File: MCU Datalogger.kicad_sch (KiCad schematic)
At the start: 0 parts

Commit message: symbols initialized
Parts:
- added BT?: Battery_Cell, symbol Device:Battery_Cell
- added C1, C2, C3, C?: C, symbol Device:C
- added C?: C_Polarized, symbol Device:C_Polarized
- added D1, D?: LED, symbol Device:LED
- added H1, H2, H3, H?: MountingHole, symbol Mechanical:MountingHole
- added R1, R2, R3, R4, R5, R6, R?: R, symbol Device:R
- added U1, U?: 24LC1025, symbol Memory_EEPROM:24LC1025
- added U?: ATMEGA328PB-AU, 32A_MCH, symbol 2025-06-18_17-37-05:ATMEGA328PB-AU
- added U?: DS1337S_, DS1337S_:SOIC127P600X175-8N, symbol DS1337S_:DS1337S_
- added Y1, Y?: Crystal, symbol Device:Crystal
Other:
- added sheet connnector sheet (connector.kicad_sch)

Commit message: symbols updated
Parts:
- removed U?: ATMEGA328PB-AU, 32A_MCH, symbol 2025-06-18_17-37-05:ATMEGA328PB-AU
- added U?: ATMEGA328P-AU, TQFP32_32A_MCH, symbol 2025-06-19_06-22-11:ATMEGA328P-AU
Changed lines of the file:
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@@
-	)
-	(symbol
-		(lib_id "2025-06-18_17-37-05:ATMEGA328PB-AU")
-		(at 143.51 46.99 0)
-		(unit 1)
-		(exclude_from_sim no)
-		(in_bom yes)
-		(on_board yes)
-		(dnp no)
-		(fields_autoplaced yes)
-		(property "Reference" "U?"
-			(at 209.55 36.83 0)
-			(effects
-				(font
-					(size 1.524 1.524)
-				)
-			)
-		)
-		(property "Value" "ATMEGA328PB-AU"
-			(at 209.55 39.37 0)
-			(effects
-				(font
-					(size 1.524 1.524)
-				)
-			)
-		)
-		(property "Footprint" "32A_MCH"
-			(at 143.51 46.99 0)
-			(effects
-				(font
-					(size 1.27 1.27)
-					(italic yes)
-				)
-				(hide yes)
-			)
-		)
-		(property "Datasheet" "ATMEGA328PB-AU"
-			(at 143.51 46.99 0)
-			(effects
-				(font
-					(size 1.27 1.27)
-					(italic yes)
-				)
-				(hide yes)
-			)
-		)
-		(property "Description" ""
-			(at 143.51 46.99 0)
-			(effects
-				(font
-					(size 1.27 1.27)
-				)
-				(hide yes)
-			)
-		)
-		(pin "9"
-		)
-		(pin "7"
-		)
-		(pin "2"
-		)
-		(pin "29"
-		)
-		(pin "27"
-		)
-		(pin "26"
-		)
-		(pin "3"
-		)
-		(pin "8"
-		)
-		(pin "1"
-		)
-		(pin "6"
-		)
-		(pin "4"
-		)
-		(pin "5"
-		)
-		(pin "11"
-		)
-		(pin "12"
-		)
-		(pin "13"
-		)
-		(pin "14"
-		)
-		(pin "15"
-		)
-		(pin "16"
-		)
-		(pin "32"
-		)
-		(pin "10"
-		)
-		(pin "31"
-		)
-		(pin "30"
-		)
-		(pin "28"
-		)
-		(pin "20"
-		)
-		(pin "23"
-		)
-		(pin "21"
-		)
-		(pin "19"
-		)
-		(pin "25"
-		)
-		(pin "18"
-		)
-		(pin "24"
-		)
-		(pin "22"
-		)
-		(pin "17"
-		)
-		(instances
-			(project ""
-				(path "/3b0fcfdb-a6be-445d-b7c4-9e7a0848a48e"
-					(reference "U?")
-					(unit 1)
-				)
-			)
-		)
 	)
 	(symbol
@@
 					(unit 1)
 				)
+			)
+		)
+	)
+	(symbol
+		(lib_id "2025-06-19_06-22-11:ATMEGA328P-AU")
+		(at 141.986 38.1 0)
+		(unit 1)
+		(exclude_from_sim no)
+		(in_bom yes)
+		(on_board yes)
+		(dnp no)
+		(fields_autoplaced yes)
+		(property "Reference" "U?"
+			(at 200.406 27.94 0)
+			(effects
+				(font
+					(size 1.524 1.524)
+				)
+			)
+		)
+		(property "Value" "ATMEGA328P-AU"
+			(at 200.406 30.48 0)
+			(effects
+				(font
+					(size 1.524 1.524)
+				)
+			)
+		)
+		(property "Footprint" "TQFP32_32A_MCH"
+			(at 141.986 38.1 0)
+			(effects
+				(font
+					(size 1.27 1.27)
+					(italic yes)
+				)
+				(hide yes)
+			)
+		)
+		(property "Datasheet" "ATMEGA328P-AU"
+			(at 141.986 38.1 0)
+			(effects
+				(font
+					(size 1.27 1.27)
+					(italic yes)
+				)
+				(hide yes)
+			)
+		)
+		(property "Description" ""
+			(at 141.986 38.1 0)
+			(effects
+				(font
+					(size 1.27 1.27)
+				)
+				(hide yes)
+			)
+		)
+		(pin "11"
+		)
+		(pin "5"
+		)
+		(pin "7"
+		)
+		(pin "1"
+		)
+		(pin "3"
+		)
+		(pin "9"
+		)
+		(pin "2"
+		)
+		(pin "4"
+		)
+		(pin "8"
+		)
+		(pin "6"
+		)
+		(pin "10"
+		)
+		(pin "12"
+		)
+		(pin "13"
+		)
+		(pin "14"
+		)
+		(pin "15"
+		)
+		(pin "16"
+		)
+		(pin "32"
+		)
+		(pin "31"
+		)
+		(pin "25"
+		)
+		(pin "29"
+		)
+		(pin "23"
+		)
+		(pin "21"
+		)
+		(pin "19"
+		)
+		(pin "20"
+		)
+		(pin "28"
+		)
+		(pin "18"
+		)
+		(pin "26"
+		)
+		(pin "17"
+		)
+		(pin "27"
+		)
+		(pin "24"
+		)
+		(pin "22"
+		)
+		(pin "30"
+		)
+		(instances
+			(project ""
+				(path "/3b0fcfdb-a6be-445d-b7c4-9e7a0848a48e"
+					(reference "U?")
+					(unit 1)
+				)

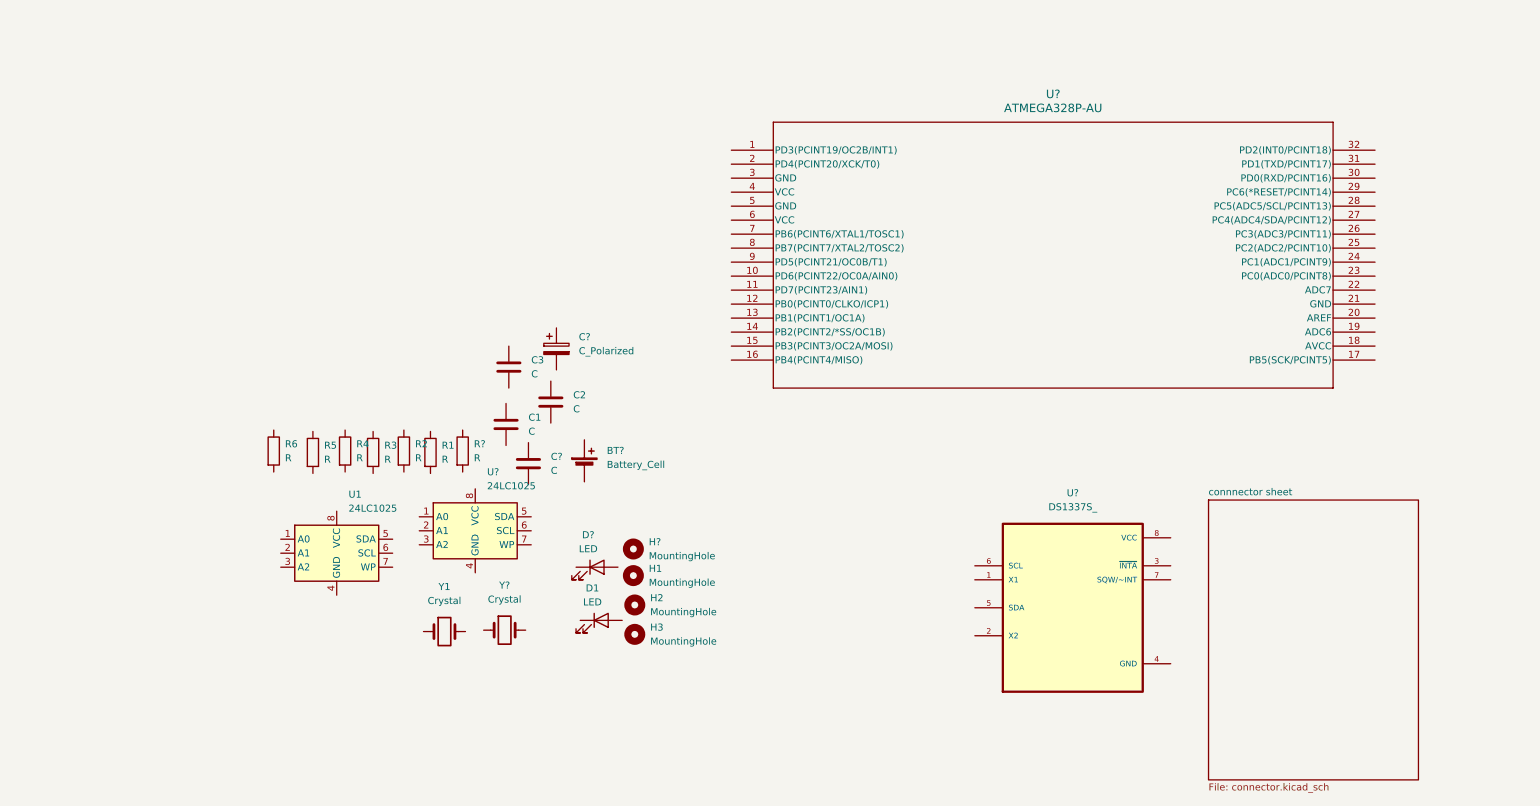
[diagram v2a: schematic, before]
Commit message: symbols arranged
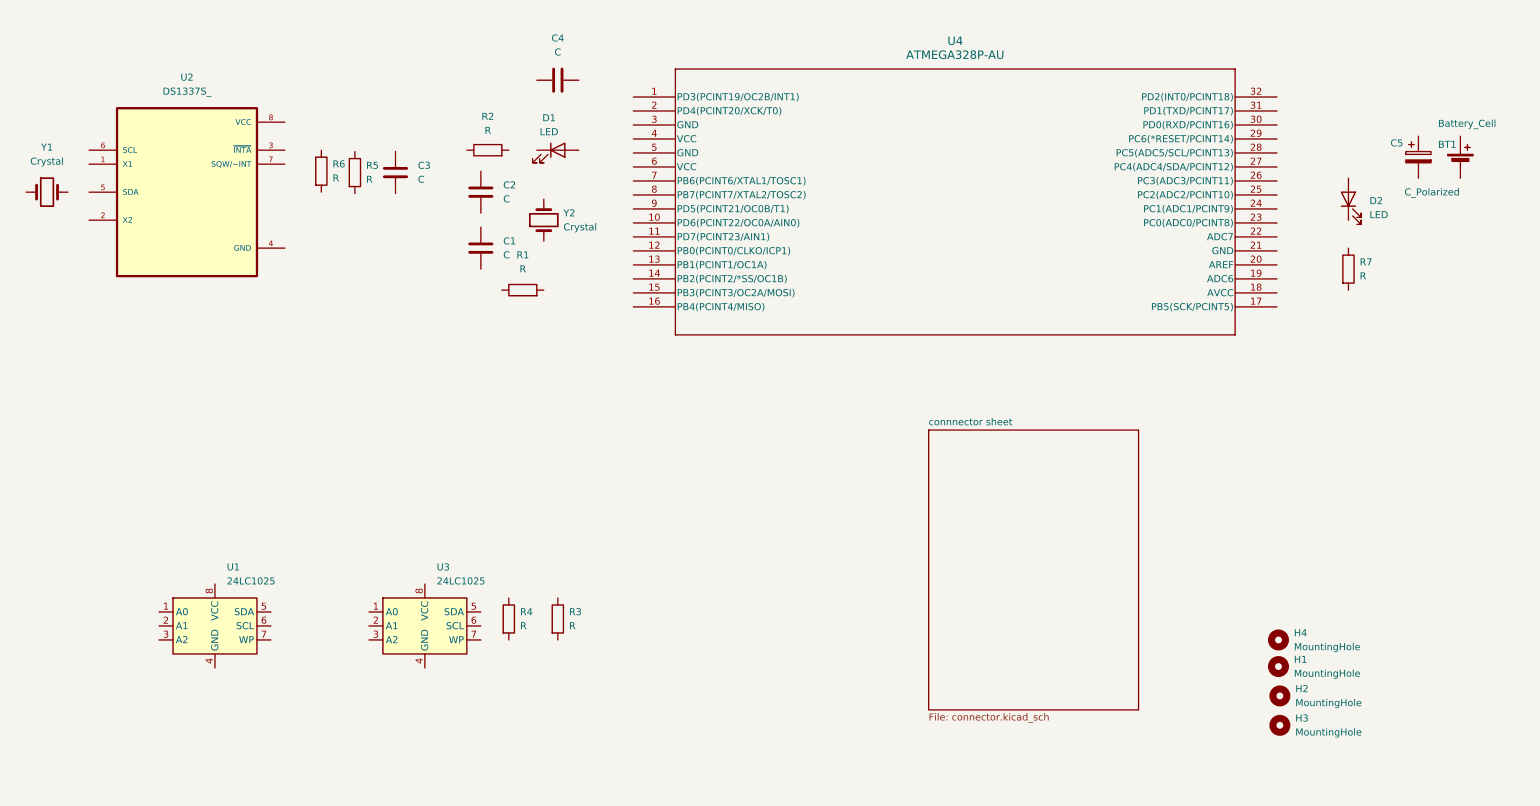
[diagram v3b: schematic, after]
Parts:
- gave numbers to parts that had none: 10
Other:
- moved on the sheet: BT1, C1, C2, C3, C4, C5, D1, D2, H1, H2, H3, H4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

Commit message: Added commponent values
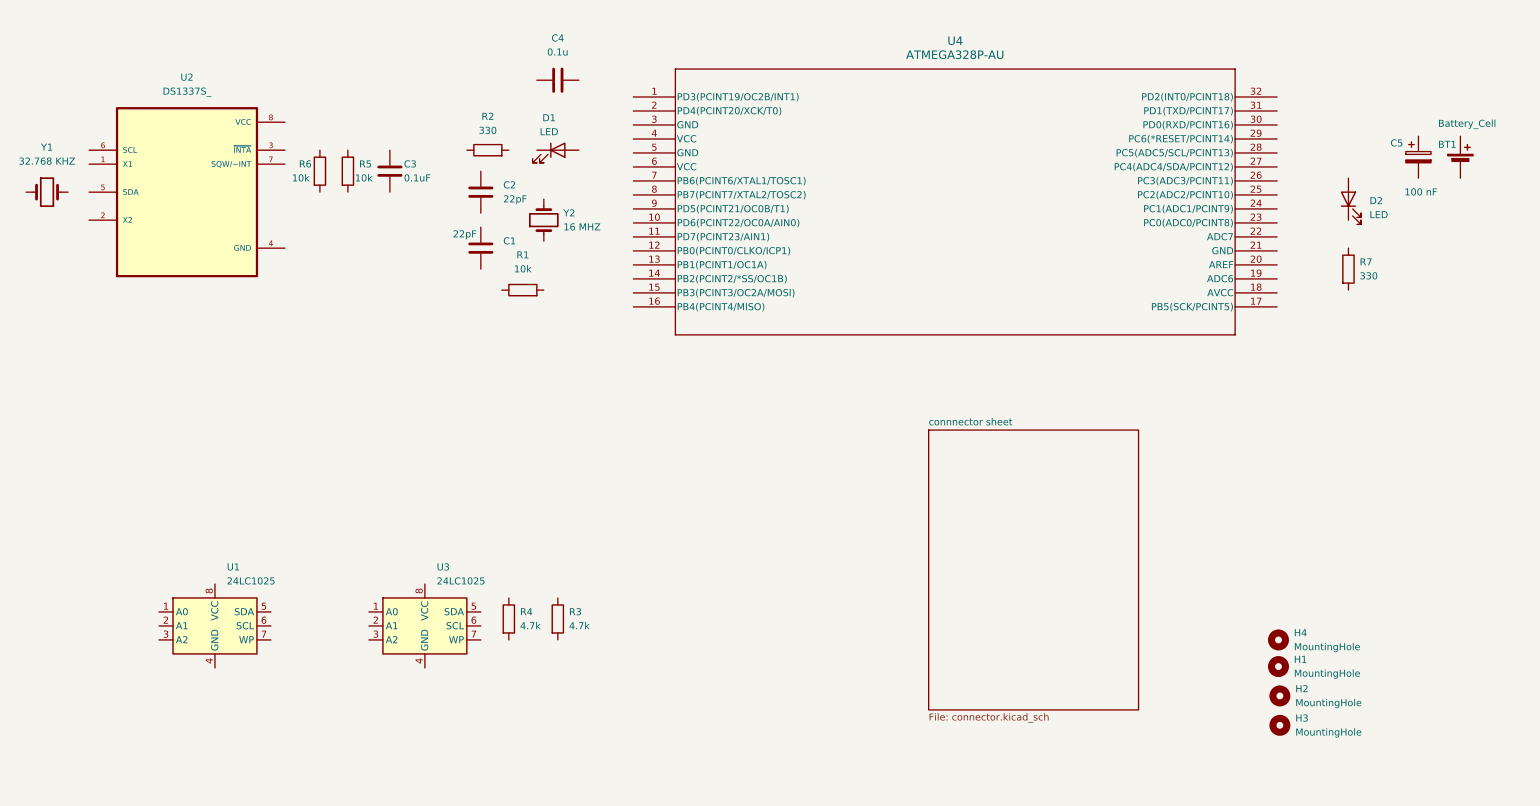
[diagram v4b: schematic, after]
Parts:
- C1, C2: value C -> 22pF
- C3: value C -> 0.1uF
- C4: value C -> 0.1u
- C5: value C_Polarized -> 100 nF
- R1, R5, R6: value R -> 10k
- R2, R7: value R -> 330
- R3, R4: value R -> 4.7k
- Y1: value Crystal -> 32.768 KHZ
- Y2: value Crystal -> 16 MHZ
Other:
- moved on the sheet: C3, R5
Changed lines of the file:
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@@
 		(on_board yes)
 		(dnp no)
-		(fields_autoplaced yes)
 		(property "Reference" "C1"
 			(at 100.584 54.6099 0)
@@
 			)
 		)
-		(property "Value" "C"
-			(at 100.584 57.1499 0)
+		(property "Value" "22pF"
+			(at 91.44 53.34 0)
 			(effects
 				(font
@@
 			)
 		)
-		(property "Value" "Crystal"
+		(property "Value" "32.768 KHZ"
 			(at 17.78 40.132 0)
 			(effects
@@
 	(symbol
 		(lib_id "Device:C")
-		(at 81.026 42.164 0)
-		(unit 1)
-		(exclude_from_sim no)
-		(in_bom yes)
-		(on_board yes)
-		(dnp no)
-		(fields_autoplaced yes)
+		(at 80.01 41.91 0)
+		(unit 1)
+		(exclude_from_sim no)
+		(in_bom yes)
+		(on_board yes)
+		(dnp no)
 		(property "Reference" "C3"
-			(at 85.09 40.8939 0)
-			(effects
-				(font
-					(size 1.27 1.27)
-				)
-				(justify left)
-			)
-		)
-		(property "Value" "C"
-			(at 85.09 43.4339 0)
-			(effects
-				(font
-					(size 1.27 1.27)
-				)
-				(justify left)
-			)
-		)
-		(property "Footprint" ""
-			(at 81.9912 45.974 0)
-			(effects
-				(font
-					(size 1.27 1.27)
-				)
-				(hide yes)
-			)
-		)
-		(property "Datasheet" "~"
-			(at 81.026 42.164 0)
+			(at 82.55 40.64 0)
+			(effects
+				(font
+					(size 1.27 1.27)
+				)
+				(justify left)
+			)
+		)
+		(property "Value" "0.1uF"
+			(at 82.55 43.18 0)
+			(effects
+				(font
+					(size 1.27 1.27)
+				)
+				(justify left)
+			)
+		)
+		(property "Footprint" ""
+			(at 80.9752 45.72 0)
+			(effects
+				(font
+					(size 1.27 1.27)
+				)
+				(hide yes)
+			)
+		)
+		(property "Datasheet" "~"
+			(at 80.01 41.91 0)
 			(effects
 				(font
@@
 		)
 		(property "Description" "Unpolarized capacitor"
-			(at 81.026 42.164 0)
+			(at 80.01 41.91 0)
 			(effects
 				(font
@@
 			)
 		)
-		(property "Value" "C"
+		(property "Value" "22pF"
 			(at 100.584 46.9899 0)
 			(effects
@@
 	(symbol
 		(lib_id "Device:R")
-		(at 67.564 41.91 0)
-		(unit 1)
-		(exclude_from_sim no)
-		(in_bom yes)
-		(on_board yes)
-		(dnp no)
-		(fields_autoplaced yes)
+		(at 67.31 41.91 0)
+		(unit 1)
+		(exclude_from_sim no)
+		(in_bom yes)
+		(on_board yes)
+		(dnp no)
 		(property "Reference" "R6"
-			(at 69.596 40.6399 0)
-			(effects
-				(font
-					(size 1.27 1.27)
-				)
-				(justify left)
-			)
-		)
-		(property "Value" "R"
-			(at 69.596 43.1799 0)
-			(effects
-				(font
-					(size 1.27 1.27)
-				)
-				(justify left)
-			)
-		)
-		(property "Footprint" ""
-			(at 65.786 41.91 90)
-			(effects
-				(font
-					(size 1.27 1.27)
-				)
-				(hide yes)
-			)
-		)
-		(property "Datasheet" "~"
-			(at 67.564 41.91 0)
+			(at 63.5 40.64 0)
+			(effects
+				(font
+					(size 1.27 1.27)
+				)
+				(justify left)
+			)
+		)
+		(property "Value" "10k"
+			(at 62.23 43.18 0)
+			(effects
+				(font
+					(size 1.27 1.27)
+				)
+				(justify left)
+			)
+		)
+		(property "Footprint" ""
+			(at 65.532 41.91 90)
+			(effects
+				(font
+					(size 1.27 1.27)
+				)
+				(hide yes)
+			)
+		)
+		(property "Datasheet" "~"
+			(at 67.31 41.91 0)
 			(effects
 				(font
@@
 		)
 		(property "Description" "Resistor"
-			(at 67.564 41.91 0)
+			(at 67.31 41.91 0)
 			(effects
 				(font
@@
 			)
 		)
-		(property "Value" "C"
+		(property "Value" "0.1u"
 			(at 110.49 20.32 90)
 			(effects
@@
 			)
 		)
-		(property "Value" "C_Polarized"
+		(property "Value" "100 nF"
 			(at 264.16 45.72 0)
 			(effects
@@
 			)
 		)
-		(property "Value" "R"
+		(property "Value" "4.7k"
 			(at 103.632 124.4599 0)
 			(effects
@@
 			)
 		)
-		(property "Value" "R"
+		(property "Value" "10k"
 			(at 104.14 59.69 90)
 			(effects
@@
 			)
 		)
-		(property "Value" "Crystal"
+		(property "Value" "16 MHZ"
 			(at 111.506 52.0699 90)
 			(effects
@@
 	(symbol
 		(lib_id "Device:R")
-		(at 73.66 42.164 0)
-		(unit 1)
-		(exclude_from_sim no)
-		(in_bom yes)
-		(on_board yes)
-		(dnp no)
-		(fields_autoplaced yes)
+		(at 72.39 41.91 0)
+		(unit 1)
+		(exclude_from_sim no)
+		(in_bom yes)
+		(on_board yes)
+		(dnp no)
 		(property "Reference" "R5"
-			(at 75.692 40.8939 0)
-			(effects
-				(font
-					(size 1.27 1.27)
-				)
-				(justify left)
-			)
-		)
-		(property "Value" "R"
-			(at 75.692 43.4339 0)
-			(effects
-				(font
-					(size 1.27 1.27)
-				)
-				(justify left)
-			)
-		)
-		(property "Footprint" ""
-			(at 71.882 42.164 90)
-			(effects
-				(font
-					(size 1.27 1.27)
-				)
-				(hide yes)
-			)
-		)
-		(property "Datasheet" "~"
-			(at 73.66 42.164 0)
+			(at 74.422 40.6399 0)
+			(effects
+				(font
+					(size 1.27 1.27)
+				)
+				(justify left)
+			)
+		)
+		(property "Value" "10k"
+			(at 73.66 43.18 0)
+			(effects
+				(font
+					(size 1.27 1.27)
+				)
+				(justify left)
+			)
+		)
+		(property "Footprint" ""
+			(at 70.612 41.91 90)
+			(effects
+				(font
+					(size 1.27 1.27)
+				)
+				(hide yes)
+			)
+		)
+		(property "Datasheet" "~"
+			(at 72.39 41.91 0)
 			(effects
 				(font
@@
 		)
 		(property "Description" "Resistor"
-			(at 73.66 42.164 0)
+			(at 72.39 41.91 0)
 			(effects
 				(font
@@
 			)
 		)
-		(property "Value" "R"
+		(property "Value" "4.7k"
 			(at 112.522 124.4599 0)
 			(effects
@@
 			)
 		)
-		(property "Value" "R"
+		(property "Value" "330"
 			(at 97.79 34.544 90)
 			(effects
@@
 			)
 		)
-		(property "Value" "R"
+		(property "Value" "330"
 			(at 256.032 60.9599 0)
 			(effects

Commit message: Footprints Associated
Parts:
- BT1: footprint (none) -> Connector_PinHeader_2.54mm:PinHeader_1x02_P2.54mm_Vertical
- C1, C2, C3, C4: footprint (none) -> Capacitor_SMD:C_0805_2012Metric
- C5: footprint (none) -> Capacitor_SMD:CP_Elec_3x5.3
- D1, D2: footprint (none) -> LED_SMD:LED_0805_2012Metric
- H1, H2, H3, H4: footprint (none) -> MountingHole:MountingHole_2.1mm
- R1, R2, R3, R4, R5, R6, R7: footprint (none) -> Resistor_SMD:R_0805_2012Metric
- U1, U3: footprint (none) -> Package_SO:SOIC-8_3.9x4.9mm_P1.27mm
- U2: footprint DS1337S_:SOIC127P600X175-8N -> ds1337s:SOIC127P600X175-8N
- U4: footprint TQFP32_32A_MCH -> footprints:TQFP32_32A_MCH
- Y1, Y2: footprint (none) -> Crystal:Crystal_SMD_5032-2Pin_5.0x3.2mm_HandSoldering
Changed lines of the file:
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@@
 			)
 		)
-		(property "Footprint" ""
+		(property "Footprint" "Capacitor_SMD:C_0805_2012Metric"
 			(at 97.4852 59.69 0)
 			(effects
@@
 			)
 		)
-		(property "Footprint" ""
+		(property "Footprint" "Crystal:Crystal_SMD_5032-2Pin_5.0x3.2mm_HandSoldering"
 			(at 17.78 45.72 0)
 			(effects
@@
 			)
 		)
-		(property "Footprint" ""
+		(property "Footprint" "MountingHole:MountingHole_2.1mm"
 			(at 241.3 127 0)
 			(effects
@@
 			)
 		)
-		(property "Footprint" ""
+		(property "Footprint" "Capacitor_SMD:C_0805_2012Metric"
 			(at 80.9752 45.72 0)
 			(effects
@@
 			)
 		)
-		(property "Footprint" ""
+		(property "Footprint" "LED_SMD:LED_0805_2012Metric"
 			(at 110.49 38.1 0)
 			(effects
@@
 			)
 		)
-		(property "Footprint" ""
+		(property "Footprint" "LED_SMD:LED_0805_2012Metric"
 			(at 254 46.99 0)
 			(effects
@@
 			)
 		)
-		(property "Footprint" ""
+		(property "Footprint" "Capacitor_SMD:C_0805_2012Metric"
 			(at 97.4852 49.53 0)
 			(effects
@@
 			)
 		)
-		(property "Footprint" ""
+		(property "Footprint" "Resistor_SMD:R_0805_2012Metric"
 			(at 65.532 41.91 90)
 			(effects
@@
 			)
 		)
-		(property "Footprint" ""
+		(property "Footprint" "MountingHole:MountingHole_2.1mm"
 			(at 241.554 142.494 0)
 			(effects
@@
 			)
 		)
-		(property "Footprint" ""
+		(property "Footprint" "MountingHole:MountingHole_2.1mm"
 			(at 241.3 131.826 0)
 			(effects
@@
 			)
 		)
-		(property "Footprint" ""
+		(property "Footprint" "Capacitor_SMD:C_0805_2012Metric"
 			(at 114.3 24.4348 0)
 			(effects
@@
 			)
 		)
-		(property "Footprint" ""
+		(property "Footprint" "Capacitor_SMD:CP_Elec_3x5.3"
 			(at 267.6652 43.18 0)
 			(effects
@@
 			)
 		)
-		(property "Footprint" ""
+		(property "Footprint" "Resistor_SMD:R_0805_2012Metric"
 			(at 99.822 123.19 90)
 			(effects
@@
 			)
 		)
-		(property "Footprint" ""
+		(property "Footprint" "Resistor_SMD:R_0805_2012Metric"
 			(at 104.14 65.278 90)
 			(effects
@@
 			)
 		)
-		(property "Footprint" ""
+		(property "Footprint" "Connector_PinHeader_2.54mm:PinHeader_1x02_P2.54mm_Vertical"
 			(at 274.32 39.116 90)
 			(effects
@@
 			)
 		)
-		(property "Footprint" ""
+		(property "Footprint" "Package_SO:SOIC-8_3.9x4.9mm_P1.27mm"
 			(at 86.36 124.46 0)
 			(effects
@@
 			)
 		)
-		(property "Footprint" ""
+		(property "Footprint" "MountingHole:MountingHole_2.1mm"
 			(at 241.554 137.16 0)
 			(effects
@@
 			)
 		)
-		(property "Footprint" ""
+		(property "Footprint" "Package_SO:SOIC-8_3.9x4.9mm_P1.27mm"
 			(at 48.26 124.46 0)
 			(effects
@@
 			)
 		)
-		(property "Footprint" ""
+		(property "Footprint" "Crystal:Crystal_SMD_5032-2Pin_5.0x3.2mm_HandSoldering"
 			(at 107.95 50.8 0)
 			(effects
@@
 			)
 		)
-		(property "Footprint" "TQFP32_32A_MCH"
+		(property "Footprint" "footprints:TQFP32_32A_MCH"
 			(at 124.206 28.448 0)
 			(effects
@@
 			)
 		)
-		(property "Footprint" ""
+		(property "Footprint" "Resistor_SMD:R_0805_2012Metric"
 			(at 70.612 41.91 90)
 			(effects
@@
 			)
 		)
-		(property "Footprint" ""
+		(property "Footprint" "Resistor_SMD:R_0805_2012Metric"
 			(at 108.712 123.19 90)
 			(effects
@@
 			)
 		)
-		(property "Footprint" "DS1337S_:SOIC127P600X175-8N"
+		(property "Footprint" "ds1337s:SOIC127P600X175-8N"
 			(at 43.18 45.72 0)
 			(effects
@@
 			)
 		)
-		(property "Footprint" ""
+		(property "Footprint" "Resistor_SMD:R_0805_2012Metric"
 			(at 97.79 39.878 90)
 			(effects
@@
 			)
 		)
-		(property "Footprint" ""
+		(property "Footprint" "Resistor_SMD:R_0805_2012Metric"
 			(at 252.222 59.69 90)
 			(effects
